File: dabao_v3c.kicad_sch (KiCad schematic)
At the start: 46 parts, among them J1 USB_C_Receptacle_USB2.0_16P, SW1 SW_Push, SW2 SW_Push, U1 baochip1x, U3 Baochip, U4 MT3406, U5 EMS4000RSW, U6 MT3406, Y2 48.000MHz

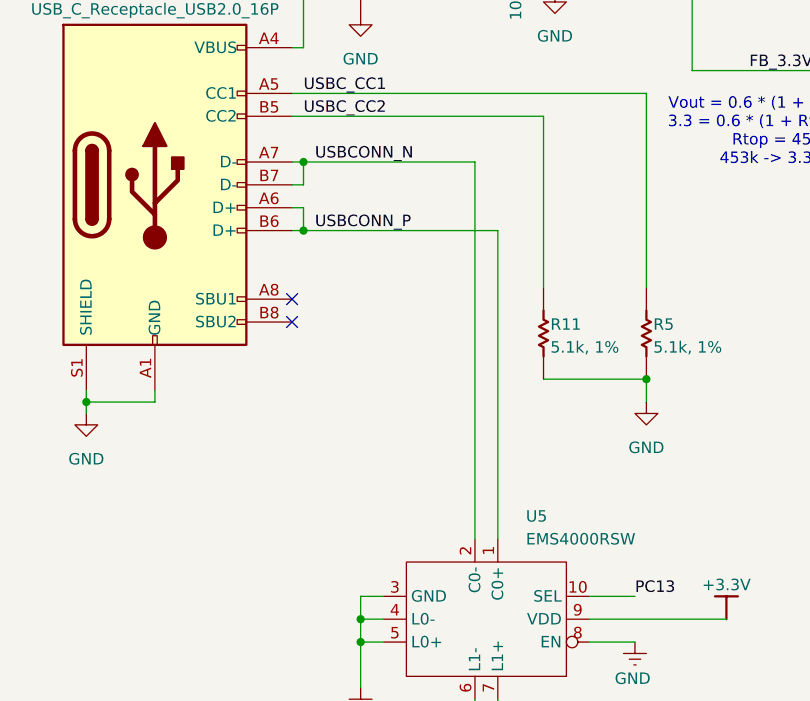
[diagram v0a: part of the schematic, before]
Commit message: add usb pads on the back side
allows for pogo testing & also possibly SMT access to USB

board designers will have to exercise caution tho - 480Mbps won't
tolerate a lot of shenanigans in layout.
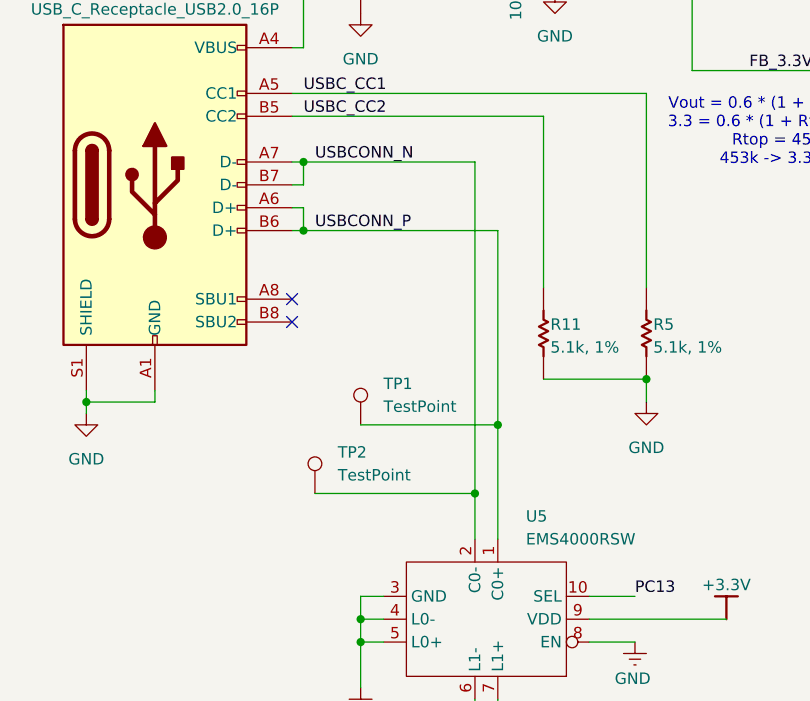
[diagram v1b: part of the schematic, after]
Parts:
- added TP1, TP2: TestPoint, TestPoint:TestPoint_Pad_D1.0mm, symbol Connector:TestPoint
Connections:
- net USBCONN_N: now also TP2.1
- net USBCONN_P: now also TP1.1
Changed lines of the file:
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@@
 	)
 	(junction
+		(at 78.74 175.26)
+		(diameter 0)
+		(color 0 0 0 0)
+	)
+	(junction
 		(at 58.42 267.97)
 		(diameter 0)
@@
 	)
 	(junction
+		(at 81.28 167.64)
+		(diameter 0)
+		(color 0 0 0 0)
+	)
+	(junction
 		(at 227.33 124.46)
 		(diameter 0)
@@
 	(wire
 		(pts
+			(xy 81.28 167.64) (xy 81.28 180.34)
+		)
+		(stroke
+			(width 0)
+			(type default)
+		)
+	)
+	(wire
+		(pts
 			(xy 162.56 260.35) (xy 193.04 260.35)
 		)
@@
 	(wire
 		(pts
+			(xy 60.96 175.26) (xy 78.74 175.26)
+		)
+		(stroke
+			(width 0)
+			(type default)
+		)
+	)
+	(wire
+		(pts
 			(xy 87.63 111.76) (xy 96.52 111.76)
 		)
@@
 	(wire
 		(pts
-			(xy 78.74 138.43) (xy 78.74 180.34)
+			(xy 78.74 138.43) (xy 78.74 175.26)
 		)
 		(stroke
@@
 	(wire
 		(pts
-			(xy 81.28 146.05) (xy 81.28 180.34)
+			(xy 81.28 146.05) (xy 81.28 167.64)
 		)
 		(stroke
@@
 	(wire
 		(pts
+			(xy 66.04 167.64) (xy 81.28 167.64)
+		)
+		(stroke
+			(width 0)
+			(type default)
+		)
+	)
+	(wire
+		(pts
 			(xy 119.38 106.68) (xy 123.19 106.68)
 		)
@@
 	(wire
 		(pts
+			(xy 78.74 175.26) (xy 78.74 180.34)
+		)
+		(stroke
+			(width 0)
+			(type default)
+		)
+	)
+	(wire
+		(pts
 			(xy 86.36 162.56) (xy 97.79 162.56)
 		)
@@
 	)
 	(symbol
+		(lib_id "Connector:TestPoint")
+		(at 66.04 167.64 0)
+		(unit 1)
+		(exclude_from_sim no)
+		(in_bom no)
+		(on_board yes)
+		(dnp no)
+		(fields_autoplaced yes)
+		(property "Reference" "TP1"
+			(at 68.58 163.0679 0)
+			(effects
+				(font
+					(size 1.27 1.27)
+				)
+				(justify left)
+			)
+		)
+		(property "Value" "TestPoint"
+			(at 68.58 165.6079 0)
+			(effects
+				(font
+					(size 1.27 1.27)
+				)
+				(justify left)
+			)
+		)
+		(property "Footprint" "TestPoint:TestPoint_Pad_D1.0mm"
+			(at 71.12 167.64 0)
+			(effects
+				(font
+					(size 1.27 1.27)
+				)
+				(hide yes)
+			)
+		)
+		(property "Datasheet" "~"
+			(at 71.12 167.64 0)
+			(effects
+				(font
+					(size 1.27 1.27)
+				)
+				(hide yes)
+			)
+		)
+		(property "Description" "test point"
+			(at 66.04 167.64 0)
+			(effects
+				(font
+					(size 1.27 1.27)
+				)
+				(hide yes)
+			)
+		)
+		(pin "1"
+		)
+		(instances
+			(project ""
+				(path "/30b97054-956f-4926-8f71-e9554821c3b2"
+					(reference "TP1")
+					(unit 1)
+				)
+			)
+		)
+	)
+	(symbol
 		(lib_id "common:root_3_Cap Semi")
 		(at 90.17 114.3 0)
@@
 					(unit 1)
 				)
+			)
+		)
+	)
+	(symbol
+		(lib_id "Connector:TestPoint")
+		(at 60.96 175.26 0)
+		(unit 1)
+		(exclude_from_sim no)
+		(in_bom no)
+		(on_board yes)
+		(dnp no)
+		(fields_autoplaced yes)
+		(property "Reference" "TP2"
+			(at 63.5 170.6879 0)
+			(effects
+				(font
+					(size 1.27 1.27)
+				)
+				(justify left)
+			)
+		)
+		(property "Value" "TestPoint"
+			(at 63.5 173.2279 0)
+			(effects
+				(font
+					(size 1.27 1.27)
+				)
+				(justify left)
+			)
+		)
+		(property "Footprint" "TestPoint:TestPoint_Pad_D1.0mm"
+			(at 66.04 175.26 0)
+			(effects
+				(font
+					(size 1.27 1.27)
+				)
+				(hide yes)
+			)
+		)
+		(property "Datasheet" "~"
+			(at 66.04 175.26 0)
+			(effects
+				(font
+					(size 1.27 1.27)
+				)
+				(hide yes)
+			)
+		)
+		(property "Description" "test point"
+			(at 60.96 175.26 0)
+			(effects
+				(font
+					(size 1.27 1.27)
+				)
+				(hide yes)
+			)
+		)
+		(pin "1"
+		)
+		(instances
+			(project "dabao_v3c"
+				(path "/30b97054-956f-4926-8f71-e9554821c3b2"
+					(reference "TP2")
+					(unit 1)
+				)
